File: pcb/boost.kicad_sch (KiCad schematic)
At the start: 11 parts

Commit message: Manufactured board
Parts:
- C? (x2): LCSC C23630 -> C98192
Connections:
- net +5V: no longer R?.1
- net EN: now also R?.1; no longer R?.2
- net GND: now also R?.2
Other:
- moved on the sheet: R?
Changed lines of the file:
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@@
   (junction (at 179.07 82.55) (diameter 0) (color 0 0 0 0)
   )
-  (junction (at 106.68 87.63) (diameter 0) (color 0 0 0 0)
-  )
   (junction (at 96.52 82.55) (diameter 0) (color 0 0 0 0)
   )
+  (junction (at 106.68 93.98) (diameter 0) (color 0 0 0 0)
+  )
   (junction (at 147.32 97.79) (diameter 0) (color 0 0 0 0)
   )
@@
     (stroke (width 0) (type default))
   )
+  (wire (pts (xy 106.68 105.41) (xy 106.68 107.95))
+    (stroke (width 0) (type default))
+  )
   (wire (pts (xy 147.32 97.79) (xy 147.32 100.33))
     (stroke (width 0) (type default))
@@
     (stroke (width 0) (type default))
   )
-  (wire (pts (xy 106.68 80.01) (xy 106.68 87.63))
+  (wire (pts (xy 106.68 93.98) (xy 106.68 97.79))
     (stroke (width 0) (type default))
   )
@@
   )
   (wire (pts (xy 96.52 92.71) (xy 96.52 95.25))
-    (stroke (width 0) (type default))
-  )
-  (wire (pts (xy 106.68 69.85) (xy 106.68 72.39))
     (stroke (width 0) (type default))
   )
@@
     )
   )
-  (symbol (lib_id "Device:R") (at 106.68 76.2 0) (unit 1)
-    (in_bom yes) (on_board yes) (dnp no) (fields_autoplaced)
-    (property "Reference" "R?" (at 109.22 75.565 0)
-      (effects (font (size 1.27 1.27)) (justify left))
-    )
-    (property "Value" "100K" (at 109.22 78.105 0)
-      (effects (font (size 1.27 1.27)) (justify left))
-    )
-    (property "Footprint" "Resistor_SMD:R_0402_1005Metric" (at 104.902 76.2 90)
-      (effects (font (size 1.27 1.27)) hide)
-    )
-    (property "Datasheet" "~" (at 106.68 76.2 0)
-      (effects (font (size 1.27 1.27)) hide)
-    )
-    (property "LCSC" "C25741" (at 106.68 76.2 0)
+  (symbol (lib_id "Device:R") (at 106.68 101.6 0) (unit 1)
+    (in_bom yes) (on_board yes) (dnp no) (fields_autoplaced)
+    (property "Reference" "R?" (at 109.22 100.965 0)
+      (effects (font (size 1.27 1.27)) (justify left))
+    )
+    (property "Value" "100K" (at 109.22 103.505 0)
+      (effects (font (size 1.27 1.27)) (justify left))
+    )
+    (property "Footprint" "Resistor_SMD:R_0402_1005Metric" (at 104.902 101.6 90)
+      (effects (font (size 1.27 1.27)) hide)
+    )
+    (property "Datasheet" "~" (at 106.68 101.6 0)
+      (effects (font (size 1.27 1.27)) hide)
+    )
+    (property "LCSC" "C25741" (at 106.68 101.6 0)
       (effects (font (size 1.27 1.27)) hide)
     )
@@
       (effects (font (size 1.27 1.27)))
     )
-    (property "LCSC" "C23630" (at 185.42 88.9 0)
+    (property "LCSC" "C98192" (at 185.42 88.9 0)
       (effects (font (size 1.27 1.27)) hide)
     )
@@
         (path "/3a5f1087-1abe-4575-9313-bd86a5e03366/1f5aaf38-830e-4ce3-b87a-a54930c92dff"
           (reference "#PWR054") (unit 1)
-        )
-      )
-    )
-  )
-  (symbol (lib_id "power:+5V") (at 106.68 69.85 0) (unit 1)
-    (in_bom yes) (on_board yes) (dnp no) (fields_autoplaced)
-    (property "Reference" "#PWR02" (at 106.68 73.66 0)
-      (effects (font (size 1.27 1.27)) hide)
-    )
-    (property "Value" "+5V" (at 106.68 66.04 0)
-      (effects (font (size 1.27 1.27)))
-    )
-    (property "Footprint" "" (at 106.68 69.85 0)
-      (effects (font (size 1.27 1.27)) hide)
-    )
-    (property "Datasheet" "" (at 106.68 69.85 0)
-      (effects (font (size 1.27 1.27)) hide)
-    )
-    (pin "1")
-    (instances
-      (project "emonHP"
-        (path "/3a5f1087-1abe-4575-9313-bd86a5e03366/1f5aaf38-830e-4ce3-b87a-a54930c92dff"
-          (reference "#PWR02") (unit 1)
         )
       )
@@
     )
   )
+  (symbol (lib_id "power:GND") (at 106.68 107.95 0) (unit 1)
+    (in_bom yes) (on_board yes) (dnp no) (fields_autoplaced)
+    (property "Reference" "#PWR02" (at 106.68 114.3 0)
+      (effects (font (size 1.27 1.27)) hide)
+    )
+    (property "Value" "GND" (at 106.68 113.03 0)
+      (effects (font (size 1.27 1.27)))
+    )
+    (property "Footprint" "" (at 106.68 107.95 0)
+      (effects (font (size 1.27 1.27)) hide)
+    )
+    (property "Datasheet" "" (at 106.68 107.95 0)
+      (effects (font (size 1.27 1.27)) hide)
+    )
+    (pin "1")
+    (instances
+      (project "emonHP"
+        (path "/3a5f1087-1abe-4575-9313-bd86a5e03366/1f5aaf38-830e-4ce3-b87a-a54930c92dff"
+          (reference "#PWR02") (unit 1)
+        )
+      )
+    )
+  )
   (symbol (lib_id "Device:C") (at 171.45 88.9 0) (unit 1)
     (in_bom yes) (on_board yes) (dnp no)
@@
       (effects (font (size 1.27 1.27)))
     )
-    (property "LCSC" "C23630" (at 171.45 88.9 0)
-      (effects (font (size 1.27 1.27)) hide)
-    )
+    (property "LCSC" "C98192" (at 171.45 88.9 0)
+      (effects (font (size 1.27 1.27)) hide)
+    )

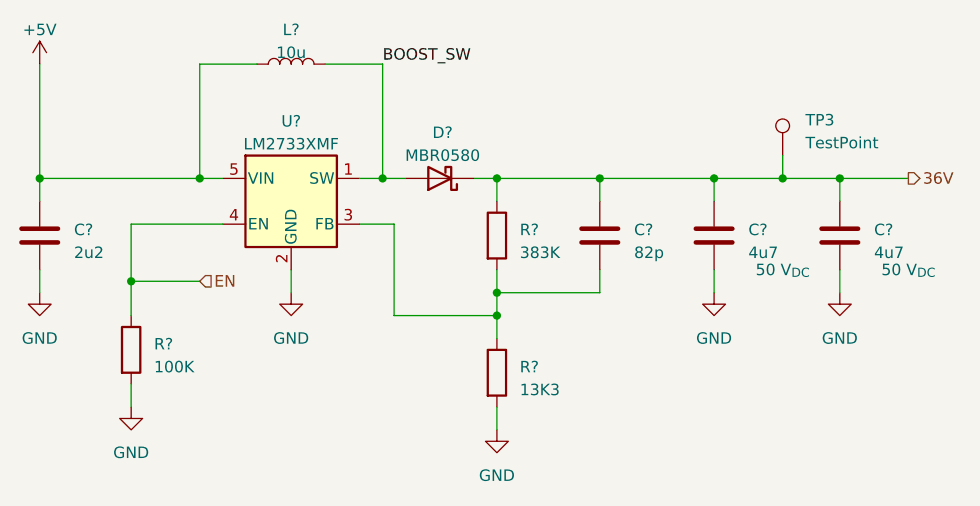
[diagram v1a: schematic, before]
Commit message: emonHP with Pi attachment
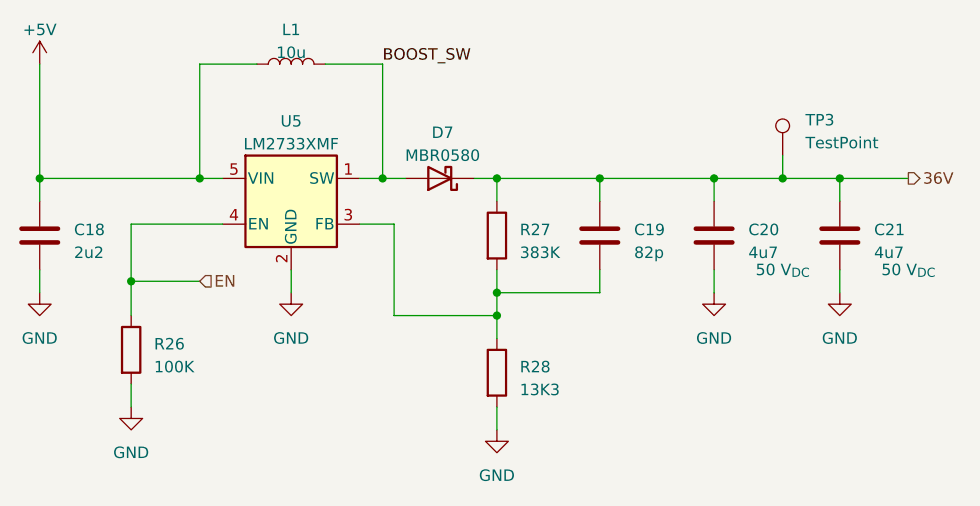
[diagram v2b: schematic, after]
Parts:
- gave numbers to parts that had none: 10
